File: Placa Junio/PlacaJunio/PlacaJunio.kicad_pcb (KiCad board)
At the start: 2 copper layers, 33 parts, among them IC1 LC86LICMD, J1 Bateria, J3 Terminal Paracaidas 2, J4 Terminal Paracaidas 1, J5 Terminal Paracaidas 3, J6 Terminal Paracaidas 4, Q2 IRLML0030, Q3 IRLML0030, Q4 IRLML0030, Q5 IRLML0030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

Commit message: Primera version
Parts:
- J3: value Terminal Paracaidas 2 -> Terminal P2
- J4: value Terminal Paracaidas 1 -> Terminal P1
- J5: value Terminal Paracaidas 3 -> Terminal P3
- J6: value Terminal Paracaidas 4 -> Terminal P4
- R14, R16, R17, R20: value 1 -> 3.3, 1%; footprint Resistor_SMD:R_0402_1005Metric -> Resistor_SMD:R_0805_2012Metric
- U2, U3: moved to B.Cu
- moved U3 82.2 mm to (112.2, 149.7), turned to 180 degrees
- moved R9 69.8 mm to (101.5, 138.4), turned to -90 degrees
- moved Q4 66.0 mm to (104.2, 138.5)
- moved C6 63.7 mm to (117.2, 125.4), turned to -90 degrees
- moved C7 60.9 mm to (114.6, 125.4), turned to -90 degrees
- moved BZ1 53.5 mm to (113.6, 144.3), turned to 90 degrees
- moved J1 50.3 mm to (81.9, 49.1), turned to 180 degrees
- moved Q2 49.7 mm to (108.3, 65.7)
- moved R18 49.2 mm to (106.6, 61.5), turned to 180 degrees
- moved R15 46.3 mm to (107.2, 50.8), turned to 180 degrees
- moved Q3 43.8 mm to (108.4, 55.4)
- moved R14 43.8 mm to (109.3, 51.5), turned to -90 degrees
- moved R5 43.6 mm to (106.6, 63.1), turned to 180 degrees
- moved R17 43.5 mm to (109.2, 61.9), turned to -90 degrees
- moved R7 43.1 mm to (107.2, 52.4), turned to 180 degrees
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
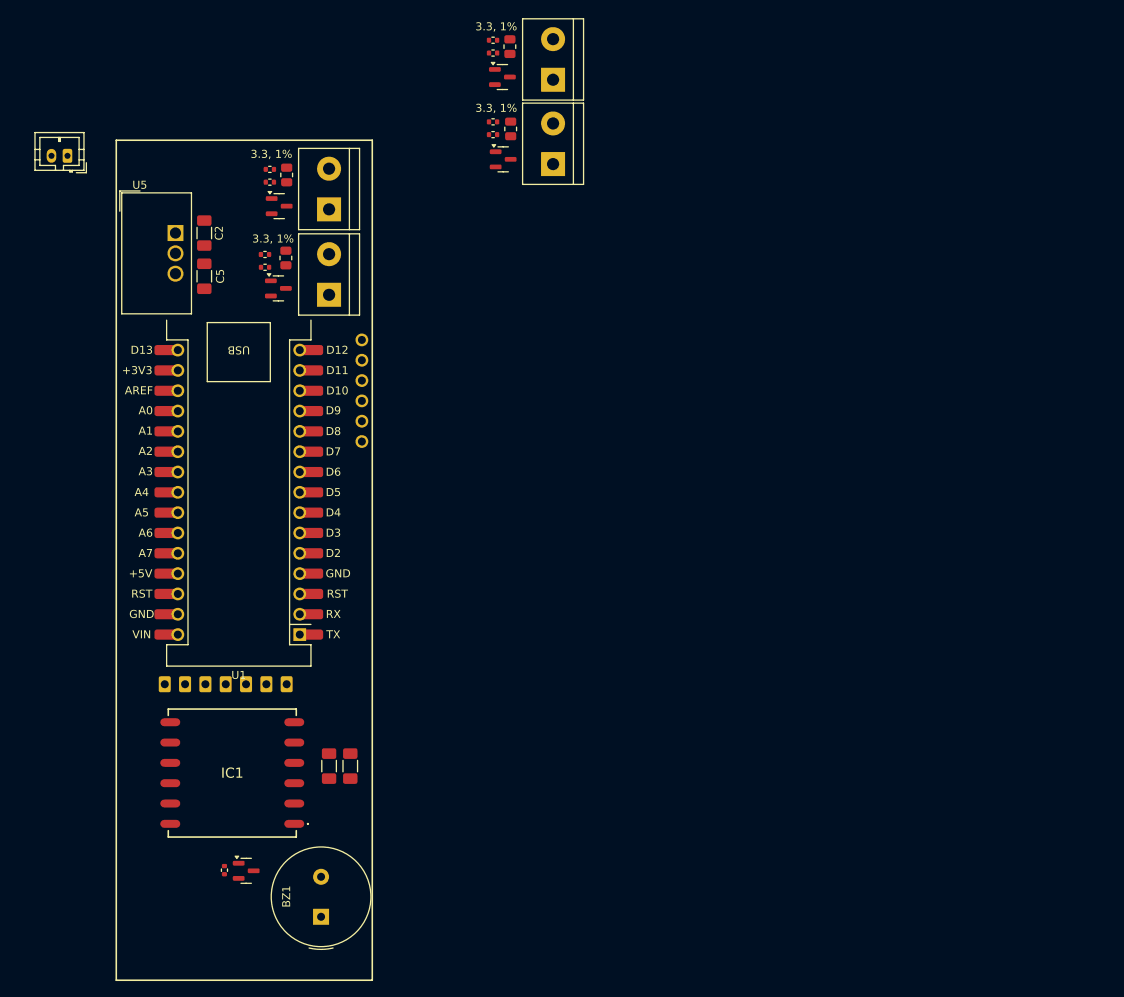
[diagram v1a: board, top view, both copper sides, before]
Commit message: Elementos posicionados
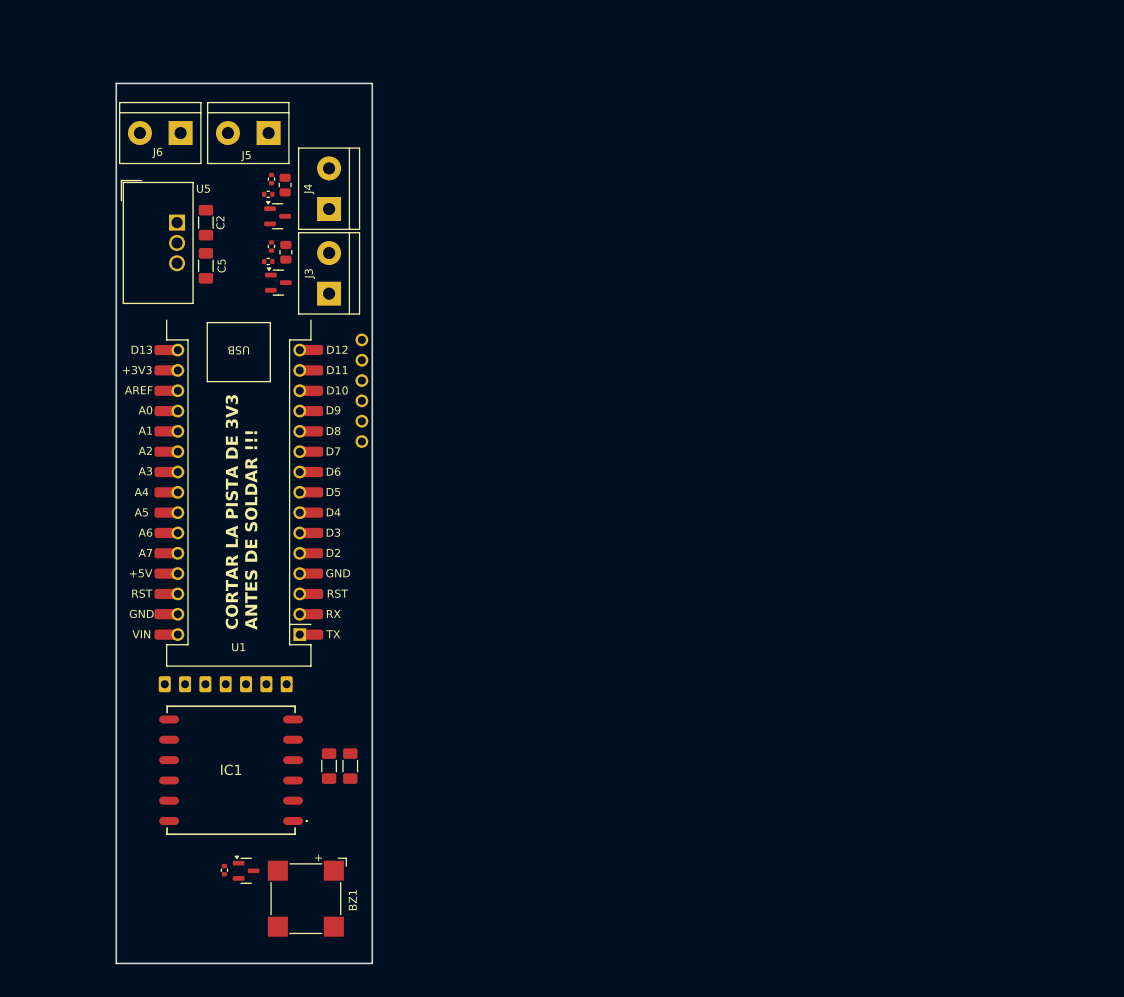
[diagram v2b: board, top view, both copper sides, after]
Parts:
- removed J1: Bateria, Connector_JST:JST_PH_B2B-PH-K_1x02_P2.00mm_Vertical
- removed Q5, Q6: IRLML0030, Package_TO_SOT_SMD:SOT-23
- removed R10, R12: 10k, Resistor_SMD:R_0402_1005Metric
- removed R16, R20: 3.3, 1%, Resistor_SMD:R_0805_2012Metric
- removed R19, R21: 1M, Resistor_SMD:R_0402_1005Metric
- BZ1: footprint Buzzer_Beeper:Buzzer_TDK_PS1240P02BT_D12.2mm_H6.5mm -> Buzzer_Beeper:MagneticBuzzer_CUI_CMT-8504-100-SMT
- R14, R17: value 3.3, 1% -> 3.3 Ohm 1%
- moved J6 46.7 mm to (96.0, 46.3), turned to 180 degrees
- moved J5 36.2 mm to (107.0, 46.3), turned to 180 degrees
- moved BZ1 2.96 mm to (111.7, 142.0), turned to -90 degrees
- moved R7 1.53 mm to (107.0, 54.0)
- moved C2 1.32 mm to (99.2, 57.5)
- moved C5 1.32 mm to (99.2, 62.9)
- moved U5 1.32 mm to (95.6, 57.5)
- moved R18 1.29 mm to (107.4, 60.5), turned to 90 degrees
- moved Q3 1.28 mm to (108.2, 56.7)
- moved R14 1.28 mm to (109.1, 52.8)
- moved R15 1.24 mm to (107.4, 52.1), turned to 90 degrees
- moved R5 0.82 mm to (107.0, 62.4)
- moved Q2 0.72 mm to (108.3, 65.0)
- moved R17 0.72 mm to (109.2, 61.2)
- moved IC1 0.38 mm to (102.3, 126.0)
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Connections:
- J5 pad 1: +3V3 -> GND
- J5 pad 2: /SENSE 3 -> Net-(J5-Pin_2)
- J6 pad 1: +3V3 -> Net-(J5-Pin_2)
- J6 pad 2: /SENSE 4 -> +BATT
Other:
- board outline added: 32 x 110 mm
- board text added: "CORTAR LA PISTA DE 3V3 ANTES DE SOLDAR !!!"

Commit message: Cambio de posición de componenentes
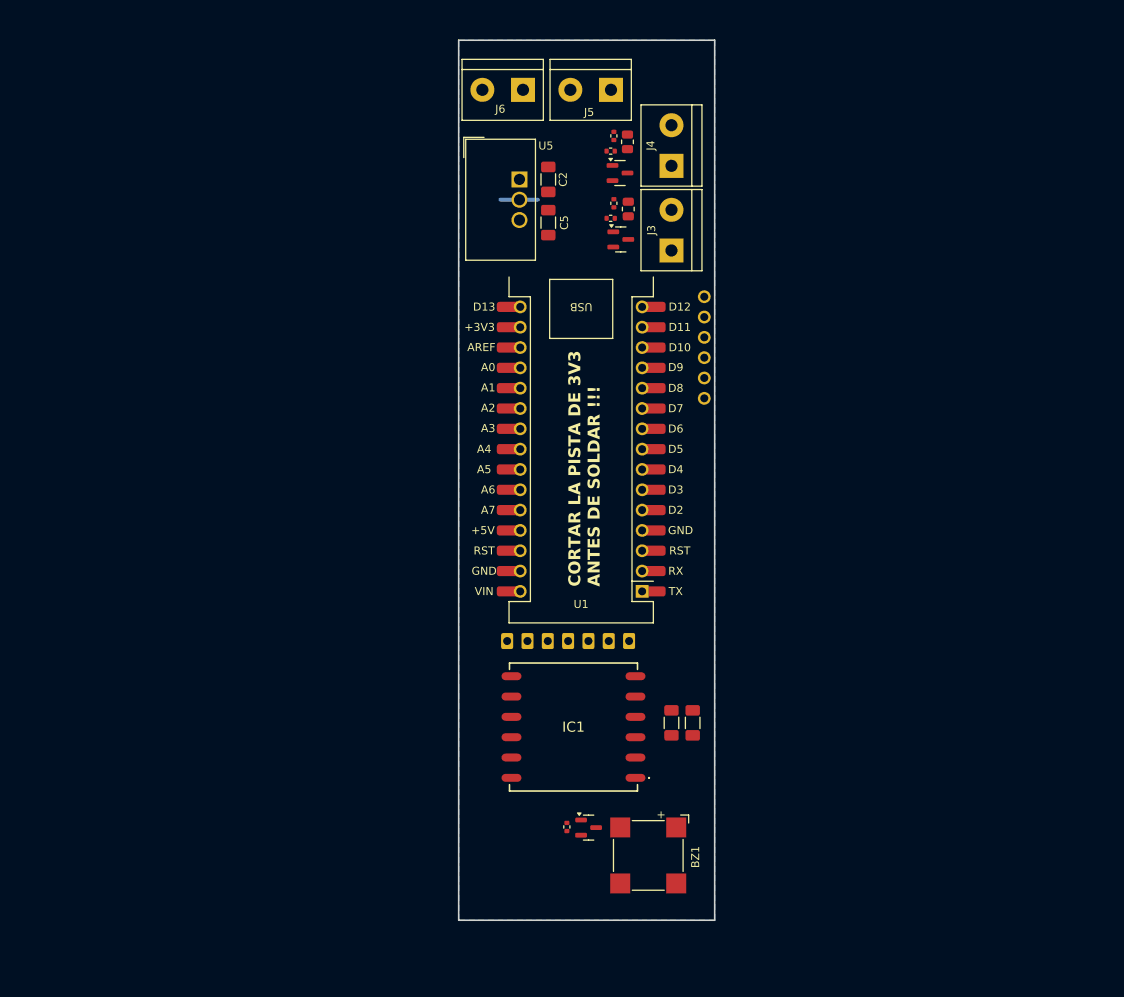
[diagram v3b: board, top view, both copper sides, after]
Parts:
- moved C6 43.1 mm to (160.1, 120.0)
- moved C7 43.1 mm to (157.4, 120.0)
- moved IC1 43.1 mm to (145.2, 120.5)
- moved J3 43.1 mm to (157.4, 61.0)
- moved J4 43.1 mm to (157.4, 50.4)
- moved Q3 43.1 mm to (151.0, 51.3)
- moved R14 43.1 mm to (151.9, 47.4)
- moved R5 43.1 mm to (149.8, 57.0)
- moved R7 43.1 mm to (149.8, 48.6)
- moved U5 43.1 mm to (138.4, 52.1)
- moved BZ1 43.1 mm to (154.5, 136.6)
- moved C2 43.1 mm to (142.0, 52.1)
- moved C5 43.1 mm to (142.0, 57.5)
- moved J5 43.1 mm to (149.8, 40.9)
- moved J6 43.1 mm to (138.8, 40.9)
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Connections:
- U1 pad 1: /SD_CS -> unconnected-(U1-D_13-Pad1)
- U1 pad 20: /RX_LoRa -> /TX_LoRa
- U1 pad 21: /TX_LoRa -> /RX_LoRa
- U1 pad 24: /PARACAIDAS 1 -> /Buzzer
- U1 pad 25: /PARACAIDAS 2 -> unconnected-(U1-D7-Pad25)
- U1 pad 26: /PARACAIDAS 3 -> unconnected-(U1-D8-Pad26)
- U1 pad 27: /PARACAIDAS 4 -> /MISO
- U1 pad 28: /MISO -> /SCK
- U1 pad 30: /SCK -> /SD_CS
- U1 pad 4: /Buzzer -> unconnected-(U1-A0-Pad4)
- U1 pad 6: /SENSE 2 -> /PARACAIDAS 1
- U1 pad 7: /SENSE 3 -> /SENSE 2
- U1 pad 8: /SENSE 4 -> /PARACAIDAS 2
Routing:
- net GND: track 0.00 -> 4.70 mm
- added copper zone on B.Cu, net GND

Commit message: Version 1
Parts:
- moved J3 26.1 mm to (136.5, 45.4), turned to -90 degrees
- moved U5 21.7 mm to (160.0, 50.3)
- moved J4 21.7 mm to (136.5, 56.1), turned to -90 degrees
- moved J6 20.1 mm to (158.7, 38.2)
- moved C2 18.5 mm to (158.5, 43.7), turned to 180 degrees
- moved R15 17.6 mm to (142.6, 62.5), turned to 0 degrees
- moved C5 16.6 mm to (158.0, 62.1), turned to 180 degrees
- moved R14 15.8 mm to (142.3, 60.0), turned to 90 degrees
- moved Q2 14.4 mm to (143.1, 47.6), turned to 180 degrees
- moved R7 11.6 mm to (144.4, 58.8), turned to 0 degrees
- moved R17 10.8 mm to (142.2, 51.4), turned to 90 degrees
- moved Q4 9.53 mm to (137.5, 132.3)
- moved R9 9.53 mm to (134.8, 132.2)
- moved BZ1 9.53 mm to (145.0, 135.8)
- moved Q3 9.10 mm to (143.2, 56.1), turned to 180 degrees
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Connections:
- J5 pad 1: GND -> Net-(J5-Pin_1)
- J5 pad 2: Net-(J5-Pin_2) -> GND
- J6 pad 1: Net-(J5-Pin_2) -> +BATT
- J6 pad 2: +BATT -> Net-(J5-Pin_1)
- U1 pad 1: unconnected-(U1-D_13-Pad1) -> /Buzzer
- U1 pad 10: unconnected-(U1-A6-Pad10)_1 -> /M1_LoRa
- U1 pad 11: unconnected-(U1-A7-Pad11)_1 -> /M0_LoRa
- U1 pad 20: /TX_LoRa -> unconnected-(U1-D2-Pad20)
- U1 pad 21: /RX_LoRa -> unconnected-(U1-D3-Pad21)_1
- U1 pad 22: /M1_LoRa -> unconnected-(U1-D4-Pad22)
- U1 pad 23: /M0_LoRa -> unconnected-(U1-D5-Pad23)_1
- U1 pad 24: /Buzzer -> unconnected-(U1-D6-Pad24)
- U1 pad 25: unconnected-(U1-D7-Pad25) -> /PARACAIDAS 1
- U1 pad 26: unconnected-(U1-D8-Pad26) -> /PARACAIDAS 2
- U1 pad 4: unconnected-(U1-A0-Pad4) -> /SENSE 1
- U1 pad 5: /SENSE 1 -> /SENSE 2
- U1 pad 6: /PARACAIDAS 1 -> unconnected-(U1-A2-Pad6)_1
- U1 pad 7: /SENSE 2 -> unconnected-(U1-A3-Pad7)_1
- U1 pad 8: /PARACAIDAS 2 -> /TX_LoRa
- U1 pad 9: unconnected-(U1-A5-Pad9) -> /RX_LoRa
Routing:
- net +3V3: track 0.00 -> 108.8 mm
- net /Buzzer: track 0.00 -> 73.0 mm
- net /SENSE 2: track 0.00 -> 41.3 mm, vias 0 -> 2
- net /PARACAIDAS 2: track 0.00 -> 37.0 mm, vias 0 -> 4
- net /TX_GPS: track 0.00 -> 34.5 mm, vias 0 -> 1
- net /RX_GPS: track 0.00 -> 34.1 mm, vias 0 -> 1
- net /PARACAIDAS 1: track 0.00 -> 31.3 mm, vias 0 -> 6
- net /TX_LoRa: track 0.00 -> 28.6 mm
- net /RX_LoRa: track 0.00 -> 25.6 mm
- net /SENSE 1: track 0.00 -> 23.0 mm, vias 0 -> 2
- net /M1_LoRa: track 0.00 -> 22.7 mm
- net /M0_LoRa: track 0.00 -> 19.6 mm
- net GND: track 4.70 -> 22.5 mm, vias 0 -> 31
- net /SD_CS: track 0.00 -> 6.28 mm
- net /SCK: track 0.00 -> 6.28 mm
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- added copper zone on F.Cu, net +3V3
- added copper zone on F.Cu, net +BATT
- added copper zone on F.Cu, net GND
- added copper zone on F.Cu, net Net-(J5-Pin_1)
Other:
- board size 32 x 110 mm -> 32 x 112.4 mm
- board text added: "+"
- board text added: "-"
- board text added: "ARMADO"

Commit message: Primera versión definitiva
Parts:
- added J1: Conn_01x07_Pin, Connector_PinHeader_2.54mm:PinHeader_1x07_P2.54mm_Vertical, F.Cu at (161.0, 81.4)
- moved R9 1.10 mm to (134.8, 133.3)
- moved BZ1 1.10 mm to (145.0, 136.9)
- moved Q4 1.10 mm to (137.5, 133.4)
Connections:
- U1 pad 20: unconnected-(U1-D2-Pad20) -> /D2
- U1 pad 21: unconnected-(U1-D3-Pad21)_1 -> /D3
- U1 pad 22: unconnected-(U1-D4-Pad22) -> /D4
- U1 pad 23: unconnected-(U1-D5-Pad23)_1 -> /D5
- U1 pad 24: unconnected-(U1-D6-Pad24) -> /D6
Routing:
- net +3V3: track 108.8 -> 131.0 mm
- net /D6: track 0.00 -> 7.52 mm
- net /D5: track 0.00 -> 7.52 mm
- net /D4: track 0.00 -> 7.52 mm
- net /D3: track 0.00 -> 7.52 mm
- net /D2: track 0.00 -> 7.52 mm
- net GND: track 22.5 -> 17.8 mm
- net /Buzzer: track 73.0 -> 74.1 mm
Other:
- board size 32 x 112.4 mm -> 32 x 113 mm
- board text added: "3V3"

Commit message: V1
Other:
- board text added: "CORTAR EL JUMPER DE 3V3 ANTES DE SOLDAR !!!"
- board text added: "FALTA DIODO PARA EL BUZZER"
- board text added: "FALTAN SCREWHOLES"
- board text removed: "CORTAR LA PISTA DE 3V3 ANTES DE SOLDAR !!!"
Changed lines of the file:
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@@
+		)
+	)
+	(gr_text "FALTA DIODO PARA EL BUZZER\n"
+		(at 170.7 69.2 0)
+		(layer "F.SilkS")
+		(effects
+			(font
+				(size 1.5 1.5)
+				(thickness 0.3)
+				(bold yes)
+			)
+			(justify left bottom)
 		)
 	)
@@
 		)
 	)
-	(gr_text "CORTAR LA PISTA DE 3V3\nANTES DE SOLDAR !!!\n"
+	(gr_text "FALTAN SCREWHOLES"
+		(at 171 62.7 0)
+		(layer "F.SilkS")
+		(effects
+			(font
+				(size 1.5 1.5)
+				(thickness 0.3)
+				(bold yes)
+			)
+			(justify left bottom)
+		)
+	)
+	(gr_text "CORTAR EL JUMPER DE 3V3\nANTES DE SOLDAR !!!\n"
 		(at 148.6 103 90)
 		(layer "F.SilkS")

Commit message: V1 definitiva
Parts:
- added D1: D, Diode_SMD:D_0805_2012Metric, F.Cu at (146.8, 131.2)
- added H1: MountingHole, MountingHole:MountingHole_3.2mm_M3_DIN965, F.Cu at (133.2, 38.0)
- added H2: MountingHole, MountingHole:MountingHole_3.2mm_M3_DIN965, F.Cu at (161.2, 38.0)
- added H3: MountingHole, MountingHole:MountingHole_3.2mm_M3_DIN965, F.Cu at (133.2, 137.0)
- added H4: MountingHole, MountingHole:MountingHole_3.2mm_M3_DIN965, F.Cu at (161.2, 137.0)
- moved J6 3.45 mm to (155.3, 38.2)
- moved J5 2.70 mm to (144.2, 38.2)
- moved BZ1 1.99 mm to (146.8, 137.8)
- moved R9 1.80 mm to (136.6, 133.2)
- moved Q4 1.80 mm to (139.3, 133.3)
- moved U3 1.58 mm to (157.3, 144.5)
- moved U5 1.20 mm to (161.2, 50.3)
- moved J1 1.10 mm to (162.1, 81.3)
- moved U2 1.00 mm to (145.2, 63.0)
- moved J3 0.90 mm to (135.6, 45.4)
- moved J4 0.90 mm to (135.6, 56.1)
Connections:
- U1 pad 7: unconnected-(U1-A3-Pad7)_1 -> /Aux
- U3 pad 5: unconnected-(U3-AUX-Pad5) -> /Aux
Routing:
- net /Aux: track 0.00 -> 32.3 mm
- net +3V3: track 131.0 -> 136.8 mm
- net Net-(BZ1--): track 3.03 -> 7.45 mm
- net /RX_GPS: track 34.1 -> 37.6 mm, vias 1 -> 2
- net /SENSE 1: track 23.0 -> 25.4 mm
- net /Buzzer: track 74.1 -> 75.9 mm
- net /TX_GPS: track 34.5 -> 36.1 mm, vias 1 -> 2
- net /D6: track 7.52 -> 8.66 mm
- net /D5: track 7.52 -> 8.66 mm
- net /D3: track 7.52 -> 8.66 mm
- net /D2: track 7.52 -> 8.66 mm
- net /D4: track 7.52 -> 8.59 mm
- net /SENSE 2: track 41.3 -> 42.2 mm
- net /M0_LoRa: track 19.6 -> 19.0 mm
- net /M1_LoRa: track 22.7 -> 22.0 mm
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- removed copper zone on F.Cu, net GND
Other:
- board size 32 x 113 mm -> 35 x 113 mm
- board text added: "(0,0)"
- board text added: "(0,99)"
- board text added: "(28,0)"
- board text added: "(28,99)"
- board text removed: "FALTA DIODO PARA EL BUZZER"
- board text removed: "FALTAN SCREWHOLES"
